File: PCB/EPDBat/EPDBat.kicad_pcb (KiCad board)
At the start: 2 copper layers, 70 x 70 mm, 51 parts, among them J1 Conn_01x26, J10 JST-PH-SM3-TB, J2 Shelly, J3 USB-PROG, J4 Conn_01x02, J7 USB-C-Socket-V, Q1 BSS138, Q2 CJ2301, Q3 C179347, U1 TP4054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

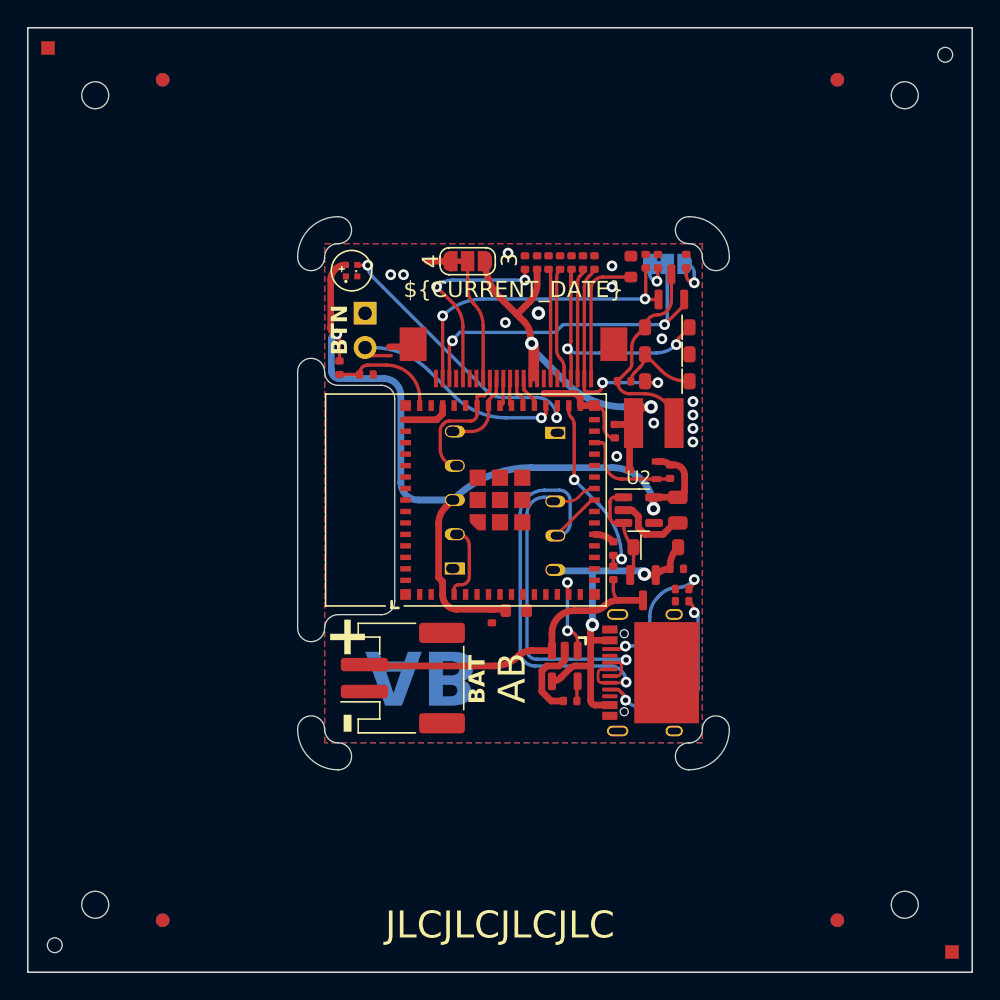
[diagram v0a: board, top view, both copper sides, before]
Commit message: Update for new USB leads
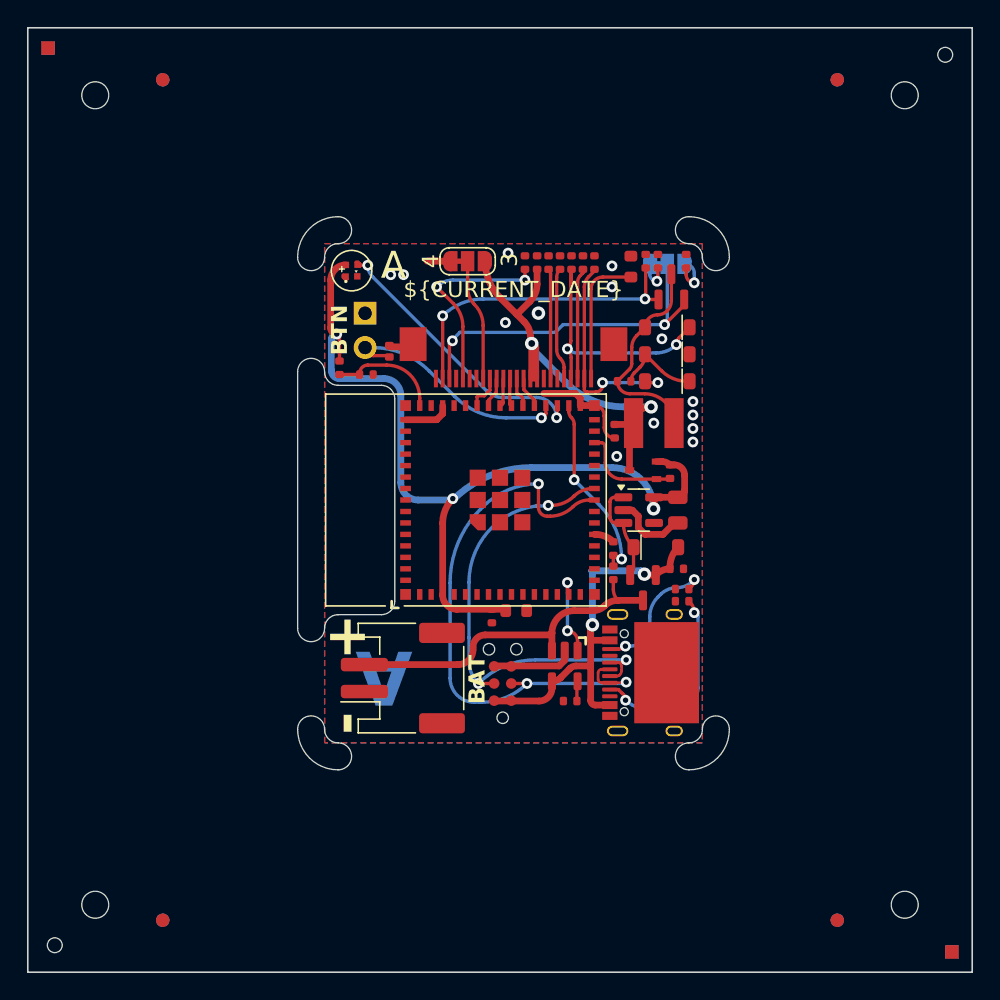
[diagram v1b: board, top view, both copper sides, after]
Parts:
- removed J2: Shelly, RevK:Shelly
- removed J3: USB-PROG, RevK:USB-PROG
- added J5: TC2030-USB-NL-DS, RevK:Tag-Connect_TC2030-IDC-NL_2x03_P1.27mm_Vertical, F.Cu at (99.2, 103.6)
- added REF**: Shadow, RevK:Shadow, F.Cu at (99.0, 90.5)
- moved J7 1.39 mm to (108.2, 102.8)
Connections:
- U4 pad 4: Net-(J2-0) -> unconnected-(U4-GPIO0-Pad4)
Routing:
- net D+: track 27.6 -> 36.7 mm, vias 1 -> 3
- net BUSY: track 9.95 -> 2.67 mm
- net D-: track 51.0 -> 43.8 mm, vias 1 -> 3
- net Net-(J2-0): track 5.60 -> 0.00 mm
- net RST: track 6.22 -> 2.21 mm
- net VBUS: track 27.5 -> 30.0 mm
- net BTN: track 17.9 -> 17.3 mm
- net +3.3V: track 65.1 -> 64.9 mm, vias 2 -> 3
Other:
- board text added: "A"
- board text removed: "AB"

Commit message: New connectors
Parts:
- moved C5 0.14 mm to (100.3, 98.3)
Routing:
- net VBUS: track 30.0 -> 29.0 mm

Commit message: No hole
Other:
- board text added: "43"
- board text added: "44"
- board text removed: "34"
- board text removed: "35"

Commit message: Update
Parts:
- removed REF**: Shadow, RevK:Shadow
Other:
- copper layers 2 -> 4

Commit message: PCB Update
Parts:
- J10: footprint Connector_JST:JST_PH_S2B-PH-SM4-TB_1x02-1MP_P2.00mm_Horizontal -> RevK:JST_PH_S2B-PH-SM4-TB_1x02-1MP_P2.00mm_Horizontal
- U2: footprint Package_TO_SOT_SMD:SOT-23-5 -> RevK:SOT-23-5-90
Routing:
- net GND: track 27.5 -> 30.2 mm
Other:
- board text removed: "BAT"
